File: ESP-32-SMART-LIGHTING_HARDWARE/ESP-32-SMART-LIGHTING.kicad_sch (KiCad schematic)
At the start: 12 parts, among them J1 PSU, J2 Screw_Terminal_01x02, J3 Screw_Terminal_01x02, Q1 IRL540N, Q2 IRL540N, U1 ESP32-S3-DEVKITC-1-N8R2, U2 INMP41, U3 INMP41

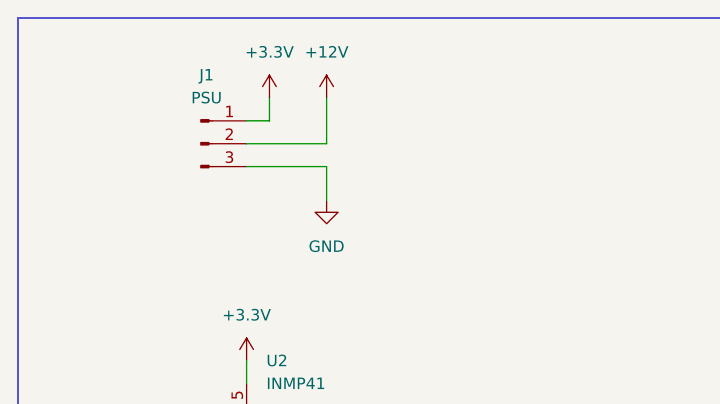
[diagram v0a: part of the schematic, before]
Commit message: Fixed PCB size, fixed module size
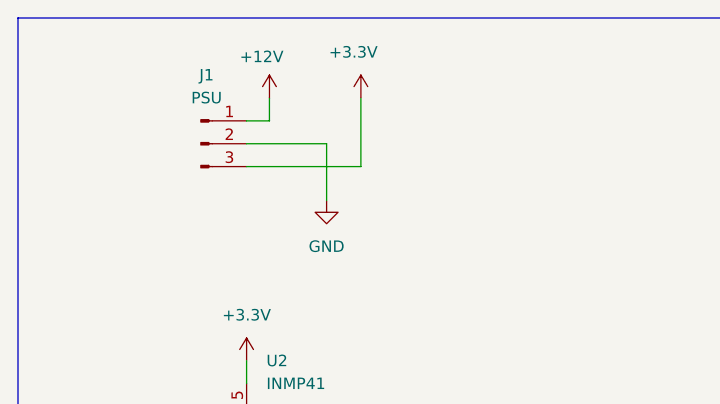
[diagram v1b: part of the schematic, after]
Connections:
- net +12V: now also J1.1 (Pin_1); no longer J1.2 (Pin_2)
- net +3.3V: now also J1.3 (Pin_3); no longer J1.1 (Pin_1)
- net GND: now also J1.2 (Pin_2); no longer J1.3 (Pin_3)
